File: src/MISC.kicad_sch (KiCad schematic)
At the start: 30 parts, among them K1 G6K-2F-Y-TR DC5, K2 G6K-2F-Y-TR DC5, Q10 BC817-40-7-F, Q6 BC817-40-7-F

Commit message: ongoing work
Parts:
- removed C88, C89: 100pF, 7Sigma:C_0402_1005Metric, symbol Capacitor:CC0402JRNPO9BN101
- removed Q10, Q6: BC817-40-7-F, 7Sigma:SOT-23-3, symbol Transistors:BC817-40-7-F
- removed R55: 10K, 7Sigma:R_0402_1005Metric, symbol Resistor:0402WGF1002TCE
- removed R56: 100K, 7Sigma:R_0402_1005Metric, symbol Resistor:0402WGF1003TCE
- removed R63, R68: 5K1, 7Sigma:R_0805_2012Metric, symbol Resistor:0805W8F5101T5E
- removed R64, R65, R66, R67: 16K, 7Sigma:R_0805_2012Metric, symbol Resistor:0805W8F1602T5E
- added Q14, Q15, Q16, Q17: SI2308A, 7Sigma:SOT-23-3, symbol Transistors:SI2308A
- added R38, R40: 374K, 7Sigma:R_0402_1005Metric, symbol Resistor:0402WGF3743TCE
- added R69: 10K, 7Sigma:R_0402_1005Metric, symbol Resistor:0402WGF1002TCE
- added R70: 100K, 7Sigma:R_0402_1005Metric, symbol Resistor:0402WGF1003TCE
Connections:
- net RY2_CTRL is gone; now on net 5V0: R61.1
- net 5V0: now also R69.1
- net GND: now also Q14.2 (S), Q15.2 (S), Q16.2 (S), Q17.2 (S), R38.2, R40.2, R70.2
- net at D6.2 (A), K1.1, R57.2: now also Q15.3 (D)
- net at R61.2, R62.1: now also Q14.1 (G), Q16.3 (D)
- net at D9.2 (A), K2.1, R60.2: now also Q14.3 (D)
- new net: Q15.1 (G), Q17.3 (D), R69.2, R70.1
- new net R1_CTRL: Q17.1 (G), R40.1
- new net R2_CTRL: Q16.1 (G), R38.1
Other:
- note removed: "- DS18B20 - extra modbus - 2x NO RY - xDI (no potential)"
- moved on the sheet: C80, C84, D1, D10, D5, D6, D8, D9, K1, K2, R57, R60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

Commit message: Layout progress
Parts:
- C24: Price @1 USD (none) -> 0.0308; Price @100 USD (none) -> 0.0308; Price @Bulk USD (none) -> 0.0209; Price Bulk Qty (none) -> 600; Price Source (none) -> LCSC; Price Updated (none) -> 2026-05-14
- C80, C84: Price @1 USD (none) -> 0.0690; Price @100 USD (none) -> 0.0561; Price @Bulk USD (none) -> 0.0494; Price Bulk Qty (none) -> 300; Price Source (none) -> LCSC; Price Updated (none) -> 2026-05-14
- D1, D10: Price @1 USD (none) -> 0.1072; Price @100 USD (none) -> 0.0867; Price @Bulk USD (none) -> 0.0688; Price Bulk Qty (none) -> 500; Price Source (none) -> LCSC; Price Updated (none) -> 2026-05-14
- D5, D8: Price @1 USD (none) -> 0.0396; Price @100 USD (none) -> 0.0396; Price @Bulk USD (none) -> 0.0266; Price Bulk Qty (none) -> 600; Price Source (none) -> LCSC; Price Updated (none) -> 2026-05-14
- D6, D9: Price @1 USD (none) -> 0.0278; Price @100 USD (none) -> 0.0278; Price @Bulk USD (none) -> 0.0193; Price Bulk Qty (none) -> 600; Price Source (none) -> LCSC; Price Updated (none) -> 2026-05-14
- K1, K2: Price @1 USD (none) -> 1.0385; Price @100 USD (none) -> 0.6783; Price @Bulk USD (none) -> 0.6315; Price Bulk Qty (none) -> 900; Price Source (none) -> LCSC; Price Updated (none) -> 2026-05-14
- Q14, Q15, Q16, Q17: Price @1 USD (none) -> 0.0364; Price @100 USD (none) -> 0.0284; Price @Bulk USD (none) -> 0.0242; Price Bulk Qty (none) -> 300; Price Source (none) -> LCSC; Price Updated (none) -> 2026-05-14
- R38, R40: Price @1 USD (none) -> 0.0004; Price @100 USD (none) -> 0.0004; Price @Bulk USD (none) -> 0.0004; Price Bulk Qty (none) -> 100; Price Source (none) -> LCSC; Price Updated (none) -> 2026-05-14
- R44: Price @1 USD (none) -> 0.0011; Price @100 USD (none) -> 0.0011; Price @Bulk USD (none) -> 0.0009; Price Bulk Qty (none) -> 1000; Price Source (none) -> LCSC; Price Updated (none) -> 2026-05-14
- R49, R62, R70: Price @1 USD (none) -> 0.0009; Price @100 USD (none) -> 0.0009; Price @Bulk USD (none) -> 0.0007; Price Bulk Qty (none) -> 1000; Price Source (none) -> LCSC; Price Updated (none) -> 2026-05-14
- R50: Price @1 USD (none) -> 0.0028; Price @100 USD (none) -> 0.0028; Price @Bulk USD (none) -> 0.0022; Price Bulk Qty (none) -> 1000; Price Source (none) -> LCSC; Price Updated (none) -> 2026-05-14
- R57, R60, R61, R69: Price @1 USD (none) -> 0.0013; Price @100 USD (none) -> 0.0013; Price @Bulk USD (none) -> 0.0011; Price Bulk Qty (none) -> 1000; Price Source (none) -> LCSC; Price Updated (none) -> 2026-05-14
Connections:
- no-connect marks 0 -> 8

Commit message: PCB layout continued
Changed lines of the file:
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@@
 		)
 		(property "Value" "SMAJ28CA"
-			(at 197.104 29.21 0)
+			(at 194.056 28.956 0)
 			(show_name no)
 			(do_not_autoplace no)
@@
 		)
 		(property "Value" "G6K-2F-Y-TR DC5"
-			(at 175.26 49.53 0)
+			(at 178.562 53.594 0)
 			(show_name no)
 			(do_not_autoplace no)
@@
 		)
 		(property "Value" "G6K-2F-Y-TR DC5"
-			(at 175.26 107.95 0)
+			(at 178.308 111.76 0)
 			(show_name no)
 			(do_not_autoplace no)
@@
 		)
 		(property "Value" "SMAJ28CA"
-			(at 197.104 87.63 0)
+			(at 194.056 87.63 0)
 			(show_name no)
 			(do_not_autoplace no)

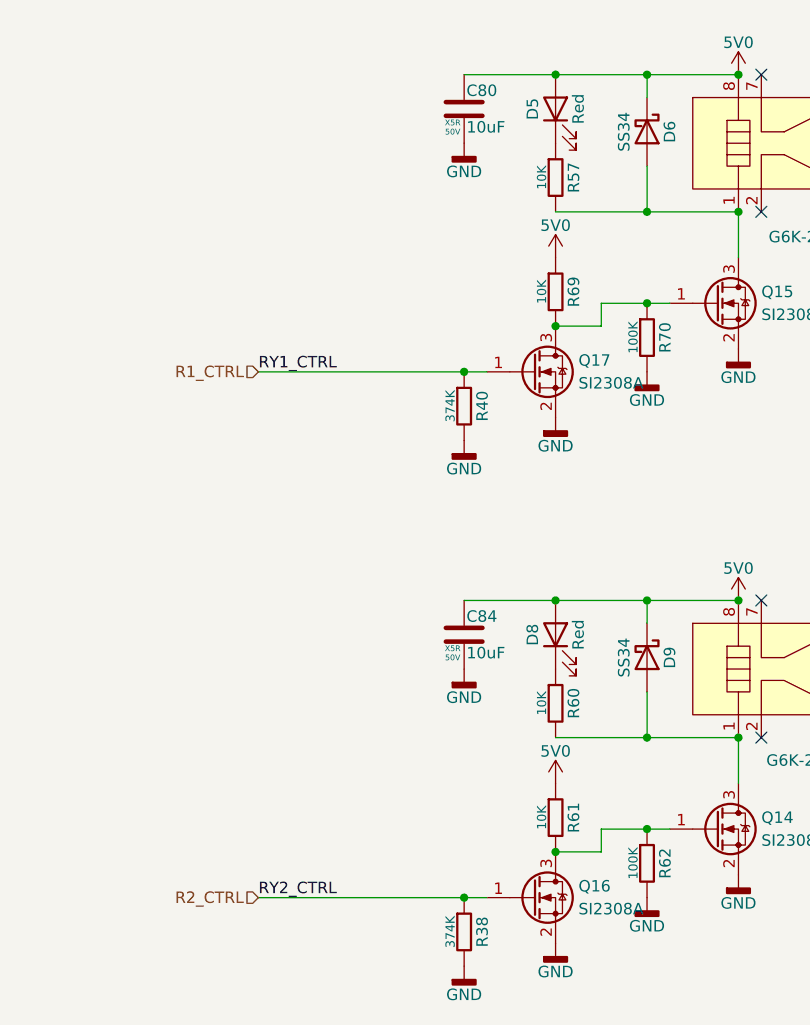
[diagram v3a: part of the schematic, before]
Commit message: schematic cleanup, verification. GPIO9 pin pulldown changed to pullup.
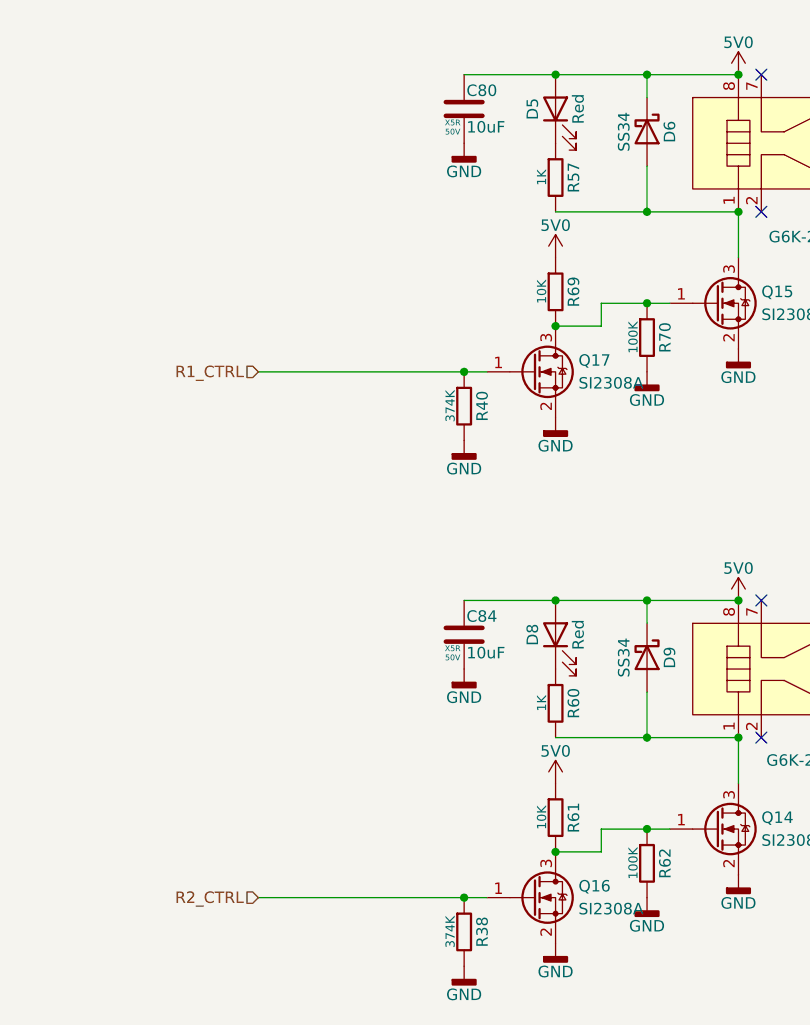
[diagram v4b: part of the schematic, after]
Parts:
- R38, R40: Supplier Part Number 1 C44358 -> C25781
- R57, R60: value 10K -> 1K; symbol Resistor:0402WGF1002TCE -> Resistor:0402WGF1001TCE; LCSC Part C25744 -> C11702; Manufacturer Part Number 1 0402WGF1002TCE -> 0402WGF1001TCE; Price @1 USD 0.0013 -> 0.0011; Price @100 USD 0.0013 -> 0.0011; Price @Bulk USD 0.0011 -> 0.0009; Supplier Part Number 1 C25744 -> C11702
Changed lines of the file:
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@@
 		)
 	)
-	(label "RY2_CTRL"
-		(at 114.3 127 0)
-		(effects
-			(font
-				(size 1.27 1.27)
-			)
-			(justify left bottom)
-		)
-	)
-	(label "RY1_CTRL"
-		(at 114.3 68.58 0)
-		(effects
-			(font
-				(size 1.27 1.27)
-			)
-			(justify left bottom)
-		)
-	)
 	(hierarchical_label "RY2_NO"
 		(shape input)
@@
 	)
 	(symbol
-		(lib_id "Resistor:0402WGF1002TCE")
+		(lib_id "Resistor:0402WGF1001TCE")
 		(at 147.32 46.99 0)
 		(unit 1)
@@
 			)
 		)
-		(property "Value" "10K"
+		(property "Value" "1K"
 			(at 145.796 46.99 90)
 			(show_name no)
@@
 			)
 		)
-		(property "Description" "10K 63mW 1% 0402"
+		(property "Description" "1K 63mW 1% 0402"
 			(at 147.32 46.99 0)
 			(hide yes)
@@
 			)
 		)
-		(property "Manufacturer Part Number 1" "0402WGF1002TCE"
+		(property "Manufacturer Part Number 1" "0402WGF1001TCE"
 			(at 147.32 46.99 0)
 			(hide yes)
@@
 			)
 		)
-		(property "Supplier Part Number 1" "C25744"
+		(property "Supplier Part Number 1" "C11702"
 			(at 147.32 46.99 0)
 			(hide yes)
@@
 			)
 		)
-		(property "LCSC Part" "C25744"
+		(property "LCSC Part" "C11702"
 			(at 147.32 46.99 0)
 			(hide yes)
@@
 			)
 		)
-		(property "Price @1 USD" "0.0013"
+		(property "Price @1 USD" "0.0011"
 			(at 147.32 46.99 0)
 			(hide yes)
@@
 			)
 		)
-		(property "Price @100 USD" "0.0013"
+		(property "Price @100 USD" "0.0011"
 			(at 147.32 46.99 0)
 			(hide yes)
@@
 			)
 		)
-		(property "Price @Bulk USD" "0.0011"
+		(property "Price @Bulk USD" "0.0009"
 			(at 147.32 46.99 0)
 			(hide yes)
@@
 			)
 		)
-		(property "Manufacturer" ""
-			(at 147.32 46.99 90)
-			(hide yes)
-			(show_name no)
-			(do_not_autoplace no)
-			(effects
-				(font
-					(size 1.27 1.27)
-				)
-			)
-		)
-		(property "Manufacturer Part Number" ""
-			(at 147.32 46.99 90)
-			(hide yes)
-			(show_name no)
-			(do_not_autoplace no)
-			(effects
-				(font
-					(size 1.27 1.27)
-				)
-			)
-		)
-		(property "on_board" ""
-			(at 147.32 46.99 90)
-			(hide yes)
-			(show_name no)
-			(do_not_autoplace no)
-			(effects
-				(font
-					(size 1.27 1.27)
-				)
-			)
-		)
 		(pin "1"
 		)
@@
 	)
 	(symbol
+		(lib_name "0402WGF3743TCE_1")
 		(lib_id "Resistor:0402WGF3743TCE")
 		(at 137.16 72.39 0)
@@
 			)
 		)
-		(property "Supplier Part Number 1" "C44358"
+		(property "Supplier Part Number 1" "C25781"
 			(at 137.16 72.39 0)
 			(hide yes)
@@
 			)
 		)
-		(property "Manufacturer" ""
-			(at 137.16 72.39 90)
-			(hide yes)
-			(show_name no)
-			(do_not_autoplace no)
-			(effects
-				(font
-					(size 1.27 1.27)
-				)
-			)
-		)
-		(property "Manufacturer Part Number" ""
-			(at 137.16 72.39 90)
-			(hide yes)
-			(show_name no)
-			(do_not_autoplace no)
-			(effects
-				(font
-					(size 1.27 1.27)
-				)
-			)
-		)
-		(property "on_board" ""
-			(at 137.16 72.39 90)
-			(hide yes)
-			(show_name no)
-			(do_not_autoplace no)
-			(effects
-				(font
-					(size 1.27 1.27)
-				)
-			)
-		)
 		(pin "1"
 		)
@@
 			)
 		)
-		(property "Supplier Part Number 1" "C44358"
+		(property "Supplier Part Number 1" "C25781"
 			(at 137.16 130.81 0)
 			(hide yes)
@@
 			)
 		)
-		(property "Manufacturer" ""
-			(at 137.16 130.81 90)
-			(hide yes)
-			(show_name no)
-			(do_not_autoplace no)
-			(effects
-				(font
-					(size 1.27 1.27)
-				)
-			)
-		)
-		(property "Manufacturer Part Number" ""
-			(at 137.16 130.81 90)
-			(hide yes)
-			(show_name no)
-			(do_not_autoplace no)
-			(effects
-				(font
-					(size 1.27 1.27)
-				)
-			)
-		)
-		(property "on_board" ""
-			(at 137.16 130.81 90)
-			(hide yes)
-			(show_name no)
-			(do_not_autoplace no)
-			(effects
-				(font
-					(size 1.27 1.27)
-				)
-			)
-		)
 		(pin "1"
 		)
@@
 	)
 	(symbol
-		(lib_id "Resistor:0402WGF1002TCE")
+		(lib_id "Resistor:0402WGF1001TCE")
 		(at 147.32 105.41 0)
 		(unit 1)
@@
 			)
 		)
-		(property "Value" "10K"
+		(property "Value" "1K"
 			(at 145.796 105.41 90)
 			(show_name no)
@@
 			)
 		)
-		(property "Description" "10K 63mW 1% 0402"
+		(property "Description" "1K 63mW 1% 0402"
 			(at 147.32 105.41 0)
 			(hide yes)
@@
 			)
 		)
-		(property "Manufacturer Part Number 1" "0402WGF1002TCE"
+		(property "Manufacturer Part Number 1" "0402WGF1001TCE"
 			(at 147.32 105.41 0)
 			(hide yes)
@@
 			)
 		)
-		(property "Supplier Part Number 1" "C25744"
+		(property "Supplier Part Number 1" "C11702"
 			(at 147.32 105.41 0)
 			(hide yes)
@@
 			)
 		)
-		(property "LCSC Part" "C25744"
+		(property "LCSC Part" "C11702"
 			(at 147.32 105.41 0)
 			(hide yes)
@@
 			)
 		)
-		(property "Price @1 USD" "0.0013"
+		(property "Price @1 USD" "0.0011"
 			(at 147.32 105.41 0)
 			(hide yes)
@@
 			)
 		)
-		(property "Price @100 USD" "0.0013"
+		(property "Price @100 USD" "0.0011"
 			(at 147.32 105.41 0)
 			(hide yes)
@@
 			)
 		)
-		(property "Price @Bulk USD" "0.0011"
+		(property "Price @Bulk USD" "0.0009"
 			(at 147.32 105.41 0)
 			(hide yes)
@@
 				)
 			)
-		)
-		(property "Manufacturer" ""
-			(at 147.32 105.41 90)
-			(hide yes)
-			(show_name no)
-			(do_not_autoplace no)
-			(effects
-				(font
-					(size 1.27 1.27)
-				)
-			)
-		)
-		(property "Manufacturer Part Number" ""
-			(at 147.32 105.41 90)
-			(hide yes)
-			(show_name no)
-			(do_not_autoplace no)
-			(effects
-				(font
-					(size 1.27 1.27)
-				)
-			)
-		)
-		(property "on_board" ""
-			(at 147.32 105.41 90)
-			(hide yes)
-			(show_name no)
-			(do_not_autoplace no)
-			(effects
-				(font
-					(size 1.27 1.27)
-				)
-			)
